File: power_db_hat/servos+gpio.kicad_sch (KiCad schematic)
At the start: 16 parts, among them J11 Conn_01x03_Pin, J12 Conn_01x03_Pin, J13 Conn_01x03_Pin, J14 Conn_01x03_Pin

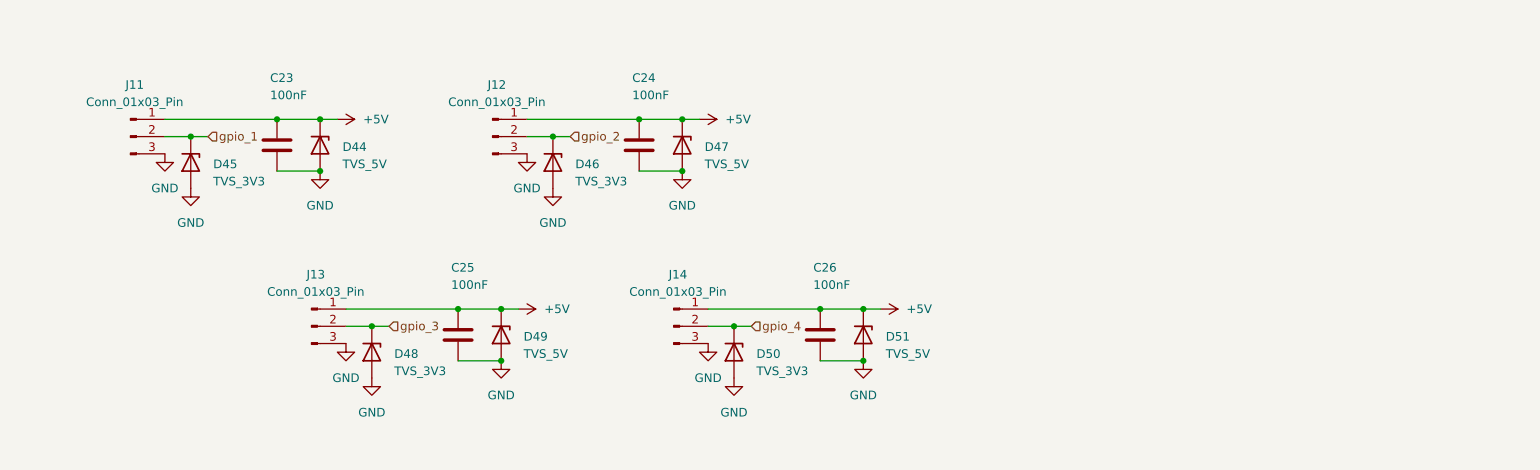
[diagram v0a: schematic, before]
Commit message: split into two PCBs
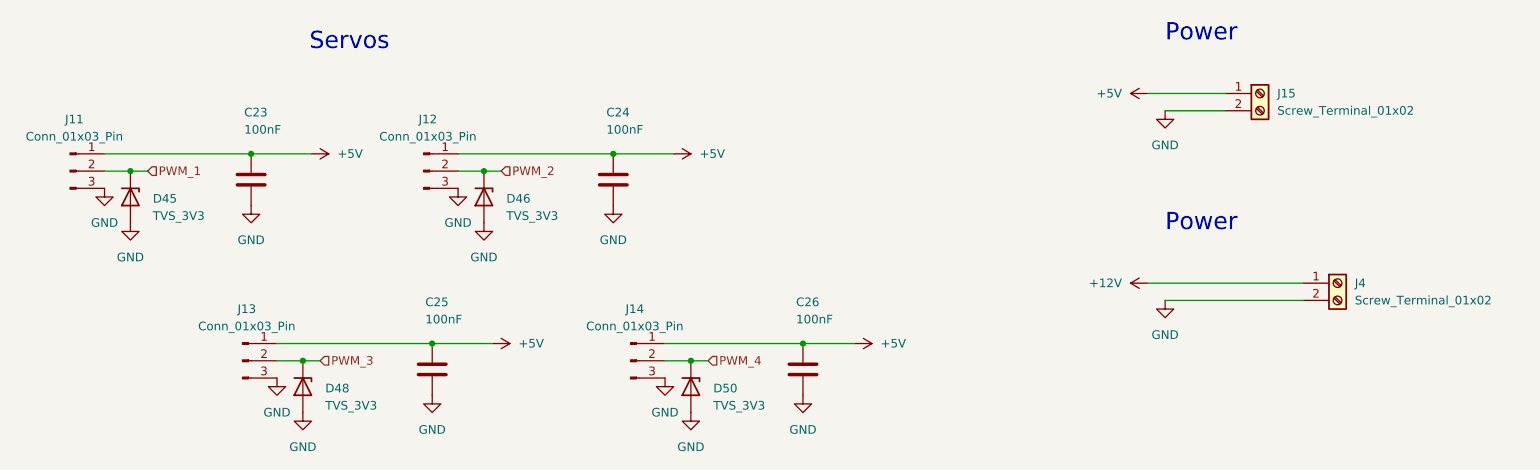
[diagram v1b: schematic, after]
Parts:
- removed D44, D47, D49, D51: TVS_5V, Diode_SMD:D_0603_1608Metric_Pad1.05x0.95mm_HandSolder, symbol Device:D_Zener
- added J15, J4: Screw_Terminal_01x02, TerminalBlock:TerminalBlock_MaiXu_MX126-5.0-02P_1x02_P5.00mm, symbol Connector:Screw_Terminal_01x02
- C23, C24, C25, C26: footprint (none) -> Capacitor_SMD:C_0603_1608Metric_Pad1.08x0.95mm_HandSolder
- J11, J12, J13, J14: footprint (none) -> Connector:FanPinHeader_1x03_P2.54mm_Vertical
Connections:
- net +5V: now also J15.1 (Pin_1)
- net GND: now also J15.2 (Pin_2), J4.2 (Pin_2)
- net gpio_1 renamed PWM_1
- net gpio_2 renamed PWM_2
- net gpio_3 renamed PWM_3
- net gpio_4 renamed PWM_4
- new net +12V: J4.1 (Pin_1)
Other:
- note added: "Power"
- note added: "Servos"
- moved on the sheet: C23, C24, C25, C26, D45, D46, D48, D50, J11, J12, J13, J14

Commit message: lol
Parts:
- removed C25, C26: 100nF, Capacitor_SMD:C_0603_1608Metric_Pad1.08x0.95mm_HandSolder, symbol Device:C
- removed D48, D50: TVS_3V3, Diode_SMD:D_0603_1608Metric_Pad1.05x0.95mm_HandSolder, symbol Device:D_Zener
- removed J13, J14: Conn_01x03_Pin, Connector:FanPinHeader_1x03_P2.54mm_Vertical, symbol Connector:Conn_01x03_Pin
- added J1, J6: Conn_01x02_Pin, TerminalBlock:TerminalBlock_Xinya_XY308-2.54-2P_1x02_P2.54mm_Horizontal, symbol Connector:Conn_01x02_Pin
- added U2, U6: LDD-700LS, LD-700LS:SOP254P1280X930-16N, symbol LDD-700LS:LDD-700LS
- J15, J4: footprint TerminalBlock:TerminalBlock_MaiXu_MX126-5.0-02P_1x02_P5.00mm -> TerminalBlock:TerminalBlock_Xinya_XY308-2.54-2P_1x02_P2.54mm_Horizontal
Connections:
- net GND: now also U2.16 (-Vin), U6.16 (-Vin)
- new net: J1.1 (Pin_1), U2.10 (-Vout), U2.11 (NC), U2.12 (NC), U2.13 (NC), U2.15 (NC), U2.2 (NC), U2.3 (NC), U2.4 (NC), U2.5 (NC), U2.6 (NC), U2.9 (-Vout)
- new net: J1.2 (Pin_2), U2.7 (+Vout), U2.8 (+Vout)
- new net: J6.1 (Pin_1), U6.10 (-Vout), U6.11 (NC), U6.12 (NC), U6.13 (NC), U6.15 (NC), U6.2 (NC), U6.3 (NC), U6.4 (NC), U6.5 (NC), U6.6 (NC), U6.9 (-Vout)
- new net: J6.2 (Pin_2), U6.7 (+Vout), U6.8 (+Vout)
- new net +24V: U2.1 (+Vin), U6.1 (+Vin)
- new net LED_PWM_1: U2.14 (PWM_DIM)
- new net LED_PWM_2: U6.14 (PWM_DIM)
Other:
- note added: "LEDs"

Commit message: termination
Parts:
- added C5: C, symbol Device:C
- added JP11, JP12: SolderJumper_2_Open, Jumper:SolderJumper-2_P1.3mm_Open_TrianglePad1.0x1.5mm, symbol Jumper:SolderJumper_2_Open
- added K1, K2: Relay_DPDT, symbol Relay:Relay_DPDT
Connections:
- net +12V: now also JP11.1 (A)
- net +5V: now also JP12.2 (B)
- net GND: now also C5.2
- new net: C5.1, JP11.2 (B), JP12.1 (A)
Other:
- note added: "Linear Actuators"
- moved on the sheet: J1, J6, U2, U6

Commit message: update
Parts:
- removed K1, K2: Relay_DPDT, symbol Relay:Relay_DPDT
- added C10, C20, C25, C30, C44: 100nF, Capacitor_SMD:C_0603_1608Metric_Pad1.08x0.95mm_HandSolder, symbol Device:C
- added C19, C26: 22uF, Capacitor_SMD:C_0603_1608Metric_Pad1.08x0.95mm_HandSolder, symbol Device:C
- added J3, J7: Screw_Terminal_01x02, TerminalBlock:TerminalBlock_Xinya_XY308-2.54-2P_1x02_P2.54mm_Horizontal, symbol Connector:Screw_Terminal_01x02
- added JP2, JP3: SolderJumper_2_Open, Jumper:SolderJumper-2_P1.3mm_Open_TrianglePad1.0x1.5mm, symbol Jumper:SolderJumper_2_Open
- added R1, R2: 10k, Resistor_SMD:R_0603_1608Metric_Pad0.98x0.95mm_HandSolder, symbol Device:R_US
- added U8, U9: DRV8212P, Package_SON:WSON-8-1EP_2x2mm_P0.5mm_EP0.9x1.6mm_ThermalVias, symbol Driver_Motor:DRV8212P
- C5: value C -> 100nF; footprint (none) -> Capacitor_SMD:C_0603_1608Metric_Pad1.08x0.95mm_HandSolder
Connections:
- net +12V: now also JP3.1 (A)
- net +24V: now also C30.2, C44.2
- net +5V: now also JP2.2 (B)
- net GND: now also C10.2, C19.2, C20.2, C25.2, C26.2, C30.1, C44.1, U8.4 (GND), U8.9 (GND), U9.4 (GND), U9.9 (GND)
- net V_ACT: now reaches C5.1, JP11.2 (B), JP12.1 (A)
- net V_ACT: now also C19.1, C25.1, C26.1, JP2.1 (A), JP3.2 (B), U8.1 (VM), U9.1 (VM)
- net at U2.10 (-Vout), U2.11 (NC), U2.12 (NC)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: now also J1.2 (Pin_2); no longer J1.1 (Pin_1)
- net at U2.7 (+Vout), U2.8 (+Vout): now also J1.1 (Pin_1); no longer J1.2 (Pin_2)
- net at U6.10 (-Vout), U6.11 (NC), U6.12 (NC)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: now also J6.2 (Pin_2); no longer J6.1 (Pin_1)
- net at U6.7 (+Vout), U6.8 (+Vout): now also J6.1 (Pin_1); no longer J6.2 (Pin_2)
- new net: R2.1, U9.7 (~{SLEEP})
- new net: J3.1 (Pin_1), U8.2 (OUT1)
- new net: J3.2 (Pin_2), U8.3 (OUT2)
- new net: R1.1, U8.7 (~{SLEEP})
- new net: J7.1 (Pin_1), U9.2 (OUT1)
- new net: J7.2 (Pin_2), U9.3 (OUT2)
- new net +3V3: C10.1, C20.1, R1.2, R2.2, U8.8 (VCC), U9.8 (VCC)
- new net MOTOR_1_A: U8.6 (IN1)
- new net MOTOR_1_B: U8.5 (IN2)
- new net MOTOR_2_A: U9.6 (IN1)
- new net MOTOR_2_B: U9.5 (IN2)
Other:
- note added: "Select between supplies"
- moved on the sheet: C5, J1, J6, JP11, JP12, U2, U6

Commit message: lol
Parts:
- U8, U9: footprint Package_SON:WSON-8-1EP_2x2mm_P0.5mm_EP0.9x1.6mm_ThermalVias -> Package_SON:WSON-8-1EP_2x2mm_P0.5mm_EP0.9x1.6mm
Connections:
- net at U8.2 (OUT1): now also J3.2 (Pin_2); no longer J3.1 (Pin_1)
- net at U8.3 (OUT2): now also J3.1 (Pin_1); no longer J3.2 (Pin_2)
- net at J7.1 (Pin_1): now also U9.3 (OUT2); no longer U9.2 (OUT1)
- net at J7.2 (Pin_2): now also U9.2 (OUT1); no longer U9.3 (OUT2)
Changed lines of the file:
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@@
 	(wire
 		(pts
-			(xy 60.96 129.54) (xy 69.85 129.54)
+			(xy 60.96 129.54) (xy 67.31 129.54)
 		)
 		(stroke
@@
 	(wire
 		(pts
-			(xy 60.96 132.08) (xy 69.85 132.08)
+			(xy 60.96 132.08) (xy 67.31 132.08)
 		)
 		(stroke
@@
 	)
 	(symbol
+		(lib_id "Connector:Screw_Terminal_01x02")
+		(at 149.86 130.81 0)
+		(mirror x)
+		(unit 1)
+		(body_style 1)
+		(exclude_from_sim no)
+		(in_bom yes)
+		(on_board yes)
+		(in_pos_files yes)
+		(dnp no)
+		(property "Reference" "J7"
+			(at 152.4 130.8101 0)
+			(show_name no)
+			(do_not_autoplace no)
+			(effects
+				(font
+					(size 1.27 1.27)
+				)
+				(justify left)
+			)
+		)
+		(property "Value" "Screw_Terminal_01x02"
+			(at 152.4 128.2701 0)
+			(hide yes)
+			(show_name no)
+			(do_not_autoplace no)
+			(effects
+				(font
+					(size 1.27 1.27)
+				)
+				(justify left)
+			)
+		)
+		(property "Footprint" "TerminalBlock:TerminalBlock_Xinya_XY308-2.54-2P_1x02_P2.54mm_Horizontal"
+			(at 149.86 130.81 0)
+			(hide yes)
+			(show_name no)
+			(do_not_autoplace no)
+			(effects
+				(font
+					(size 1.27 1.27)
+				)
+			)
+		)
+		(property "Datasheet" ""
+			(at 149.86 130.81 0)
+			(hide yes)
+			(show_name no)
+			(do_not_autoplace no)
+			(effects
+				(font
+					(size 1.27 1.27)
+				)
+			)
+		)
+		(property "Description" "Generic screw terminal, single row, 01x02, script generated (kicad-library-utils/schlib/autogen/connector/)"
+			(at 149.86 130.81 0)
+			(hide yes)
+			(show_name no)
+			(do_not_autoplace no)
+			(effects
+				(font
+					(size 1.27 1.27)
+				)
+			)
+		)
+		(pin "1"
+		)
+		(pin "2"
+		)
+		(instances
+			(project "power_db_hat"
+				(path "/e63e39d7-6ac0-4ffd-8aa3-1841a4541b55/b7d8961d-96c8-448d-accd-96aea1343789"
+					(reference "J7")
+					(unit 1)
+				)
+			)
+		)
+	)
+	(symbol
 		(lib_id "power:GND")
 		(at 50.8 147.32 0)
@@
 	)
 	(symbol
-		(lib_id "Connector:Screw_Terminal_01x02")
-		(at 74.93 129.54 0)
-		(unit 1)
-		(body_style 1)
-		(exclude_from_sim no)
-		(in_bom yes)
-		(on_board yes)
-		(in_pos_files yes)
-		(dnp no)
-		(fields_autoplaced yes)
-		(property "Reference" "J3"
-			(at 77.47 129.5399 0)
-			(show_name no)
-			(do_not_autoplace no)
-			(effects
-				(font
-					(size 1.27 1.27)
-				)
-				(justify left)
-			)
-		)
-		(property "Value" "Screw_Terminal_01x02"
-			(at 77.47 132.0799 0)
-			(hide yes)
-			(show_name no)
-			(do_not_autoplace no)
-			(effects
-				(font
-					(size 1.27 1.27)
-				)
-				(justify left)
-			)
-		)
-		(property "Footprint" "TerminalBlock:TerminalBlock_Xinya_XY308-2.54-2P_1x02_P2.54mm_Horizontal"
-			(at 74.93 129.54 0)
-			(hide yes)
-			(show_name no)
-			(do_not_autoplace no)
-			(effects
-				(font
-					(size 1.27 1.27)
-				)
-			)
-		)
-		(property "Datasheet" ""
-			(at 74.93 129.54 0)
-			(hide yes)
-			(show_name no)
-			(do_not_autoplace no)
-			(effects
-				(font
-					(size 1.27 1.27)
-				)
-			)
-		)
-		(property "Description" "Generic screw terminal, single row, 01x02, script generated (kicad-library-utils/schlib/autogen/connector/)"
-			(at 74.93 129.54 0)
-			(hide yes)
-			(show_name no)
-			(do_not_autoplace no)
-			(effects
-				(font
-					(size 1.27 1.27)
-				)
-			)
-		)
-		(pin "1"
-		)
-		(pin "2"
-		)
-		(instances
-			(project "power_db_hat"
-				(path "/e63e39d7-6ac0-4ffd-8aa3-1841a4541b55/b7d8961d-96c8-448d-accd-96aea1343789"
-					(reference "J3")
-					(unit 1)
-				)
-			)
-		)
-	)
-	(symbol
 		(lib_id "power:GND")
 		(at 115.57 48.26 0)
@@
 			)
 		)
-		(property "Footprint" "Package_SON:WSON-8-1EP_2x2mm_P0.5mm_EP0.9x1.6mm_ThermalVias"
+		(property "Footprint" "Package_SON:WSON-8-1EP_2x2mm_P0.5mm_EP0.9x1.6mm"
 			(at 125.73 154.94 0)
 			(hide yes)
@@
 			)
 		)
-		(property "Footprint" "Package_SON:WSON-8-1EP_2x2mm_P0.5mm_EP0.9x1.6mm_ThermalVias"
+		(property "Footprint" "Package_SON:WSON-8-1EP_2x2mm_P0.5mm_EP0.9x1.6mm"
 			(at 50.8 156.21 0)
 			(hide yes)
@@
 	)
 	(symbol
+		(lib_id "Connector:Screw_Terminal_01x02")
+		(at 72.39 132.08 0)
+		(mirror x)
+		(unit 1)
+		(body_style 1)
+		(exclude_from_sim no)
+		(in_bom yes)
+		(on_board yes)
+		(in_pos_files yes)
+		(dnp no)
+		(property "Reference" "J3"
+			(at 74.93 132.0801 0)
+			(show_name no)
+			(do_not_autoplace no)
+			(effects
+				(font
+					(size 1.27 1.27)
+				)
+				(justify left)
+			)
+		)
+		(property "Value" "Screw_Terminal_01x02"
+			(at 74.93 129.5401 0)
+			(hide yes)
+			(show_name no)
+			(do_not_autoplace no)
+			(effects
+				(font
+					(size 1.27 1.27)
+				)
+				(justify left)
+			)
+		)
+		(property "Footprint" "TerminalBlock:TerminalBlock_Xinya_XY308-2.54-2P_1x02_P2.54mm_Horizontal"
+			(at 72.39 132.08 0)
+			(hide yes)
+			(show_name no)
+			(do_not_autoplace no)
+			(effects
+				(font
+					(size 1.27 1.27)
+				)
+			)
+		)
+		(property "Datasheet" ""
+			(at 72.39 132.08 0)
+			(hide yes)
+			(show_name no)
+			(do_not_autoplace no)
+			(effects
+				(font
+					(size 1.27 1.27)
+				)
+			)
+		)
+		(property "Description" "Generic screw terminal, single row, 01x02, script generated (kicad-library-utils/schlib/autogen/connector/)"
+			(at 72.39 132.08 0)
+			(hide yes)
+			(show_name no)
+			(do_not_autoplace no)
+			(effects
+				(font
+					(size 1.27 1.27)
+				)
+			)
+		)
+		(pin "1"
+		)
+		(pin "2"
+		)
+		(instances
+			(project "power_db_hat"
+				(path "/e63e39d7-6ac0-4ffd-8aa3-1841a4541b55/b7d8961d-96c8-448d-accd-96aea1343789"
+					(reference "J3")
+					(unit 1)
+				)
+			)
+		)
+	)
+	(symbol
 		(lib_id "power:GND")
 		(at 63.5 48.26 0)
@@
 					(unit 1)
 				)
-			)
-		)
-	)
-	(symbol
-		(lib_id "Connector:Screw_Terminal_01x02")
-		(at 149.86 128.27 0)
-		(unit 1)
-		(body_style 1)
-		(exclude_from_sim no)
-		(in_bom yes)
-		(on_board yes)
-		(in_pos_files yes)
-		(dnp no)
-		(fields_autoplaced yes)
-		(property "Reference" "J7"
-			(at 152.4 128.2699 0)
-			(show_name no)
-			(do_not_autoplace no)
-			(effects
-				(font
-					(size 1.27 1.27)
-				)
-				(justify left)
-			)
-		)
-		(property "Value" "Screw_Terminal_01x02"
-			(at 152.4 130.8099 0)
-			(hide yes)
-			(show_name no)
-			(do_not_autoplace no)
-			(effects
-				(font
-					(size 1.27 1.27)
-				)
-				(justify left)
-			)
-		)
-		(property "Footprint" "TerminalBlock:TerminalBlock_Xinya_XY308-2.54-2P_1x02_P2.54mm_Horizontal"
-			(at 149.86 128.27 0)
-			(hide yes)
-			(show_name no)
-			(do_not_autoplace no)
-			(effects
-				(font
-					(size 1.27 1.27)
-				)
-			)
-		)
-		(property "Datasheet" ""
-			(at 149.86 128.27 0)
-			(hide yes)
-			(show_name no)
-			(do_not_autoplace no)
-			(effects
-				(font
-					(size 1.27 1.27)
-				)
-			)
-		)
-		(property "Description" "Generic screw terminal, single row, 01x02, script generated (kicad-library-utils/schlib/autogen/connector/)"
-			(at 149.86 128.27 0)
-			(hide yes)
-			(show_name no)
-			(do_not_autoplace no)
-			(effects
-				(font
-					(size 1.27 1.27)
-				)
-			)
-		)
-		(pin "1"
-		)
-		(pin "2"
-		)
-		(instances
-			(project "power_db_hat"
-				(path "/e63e39d7-6ac0-4ffd-8aa3-1841a4541b55/b7d8961d-96c8-448d-accd-96aea1343789"
-					(reference "J7")
-					(unit 1)
-				)

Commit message: lol
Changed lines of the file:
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@@
 	(text "Select between supplies\n"
 		(exclude_from_sim no)
-		(at 72.136 100.584 0)
+		(at 92.202 87.884 0)
 		(effects
 			(font
@@
 	(text "Linear Actuators"
 		(exclude_from_sim no)
-		(at 89.408 95.25 0)
+		(at 89.408 79.248 0)
 		(effects
 			(font

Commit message: damo was here
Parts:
- removed D45, D46: TVS_3V3, Diode_SMD:D_0603_1608Metric_Pad1.05x0.95mm_HandSolder, symbol Device:D_Zener
- removed JP11, JP12: SolderJumper_2_Open, Jumper:SolderJumper-2_P1.3mm_Open_TrianglePad1.0x1.5mm, symbol Jumper:SolderJumper_2_Open
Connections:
- net +5V: now also JP2.1 (A); no longer JP2.2 (B)
- net V_ACT: now also JP2.2 (B); no longer JP2.1 (A)
